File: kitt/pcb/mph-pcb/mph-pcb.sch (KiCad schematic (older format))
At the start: 99 parts, among them J1 Screw_Terminal_01x02, J2 Screw_Terminal_01x02, U1 TLC5940NT, U2 TLC5940NT, U3 TLC5940NT, U4 TLC5940NT, U5 TLC5940NT, U6 TLC5940NT, U7 TLC5940NT

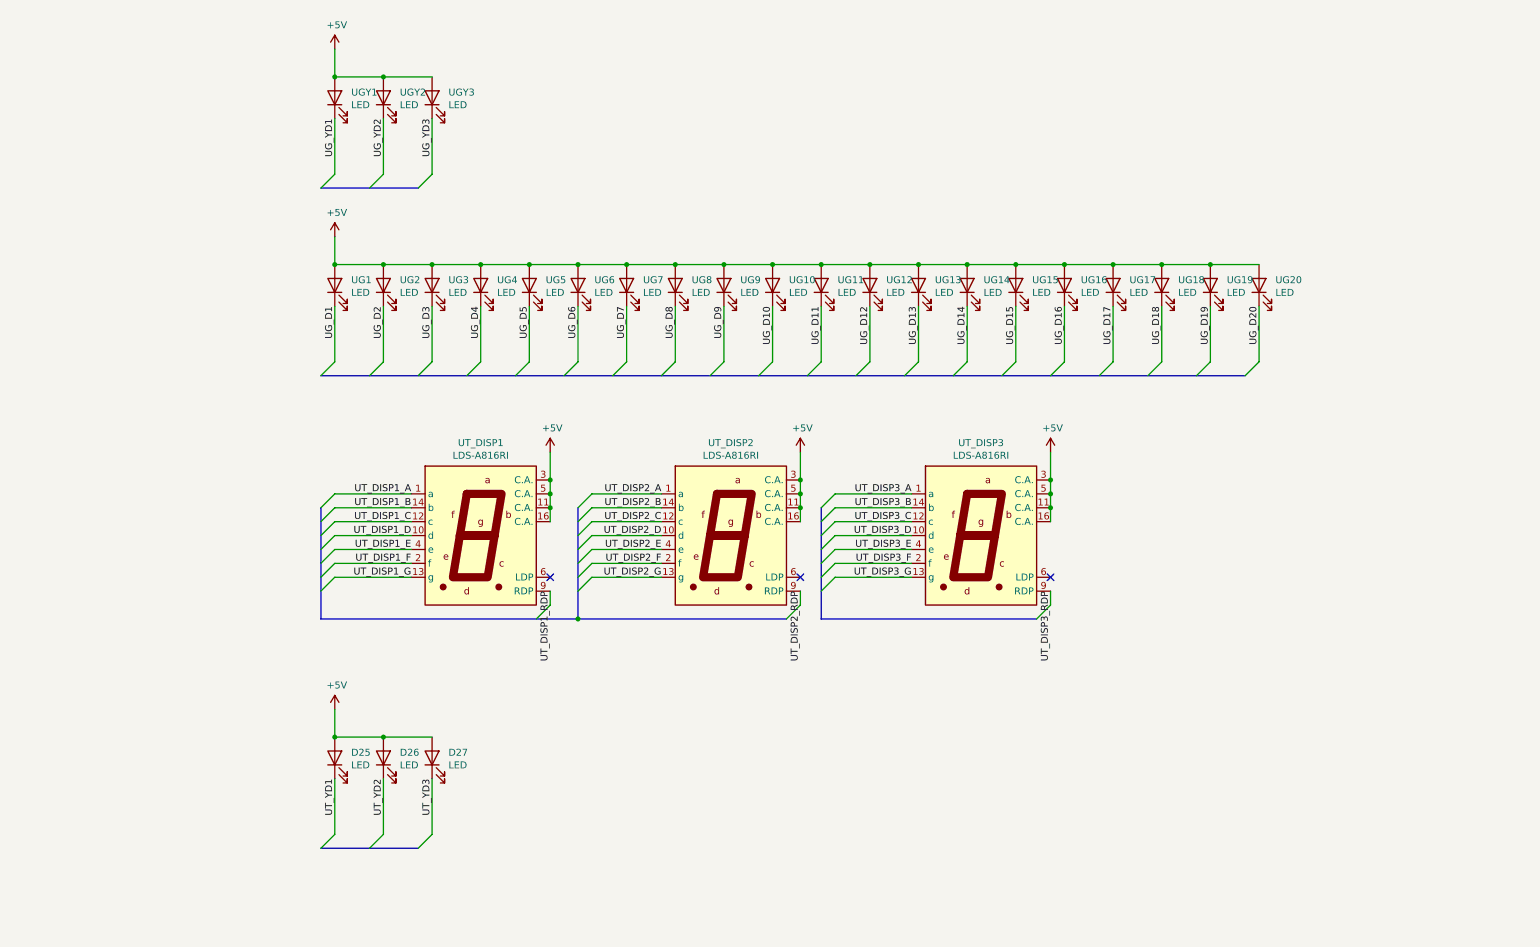
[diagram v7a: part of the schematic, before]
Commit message: added mph leds
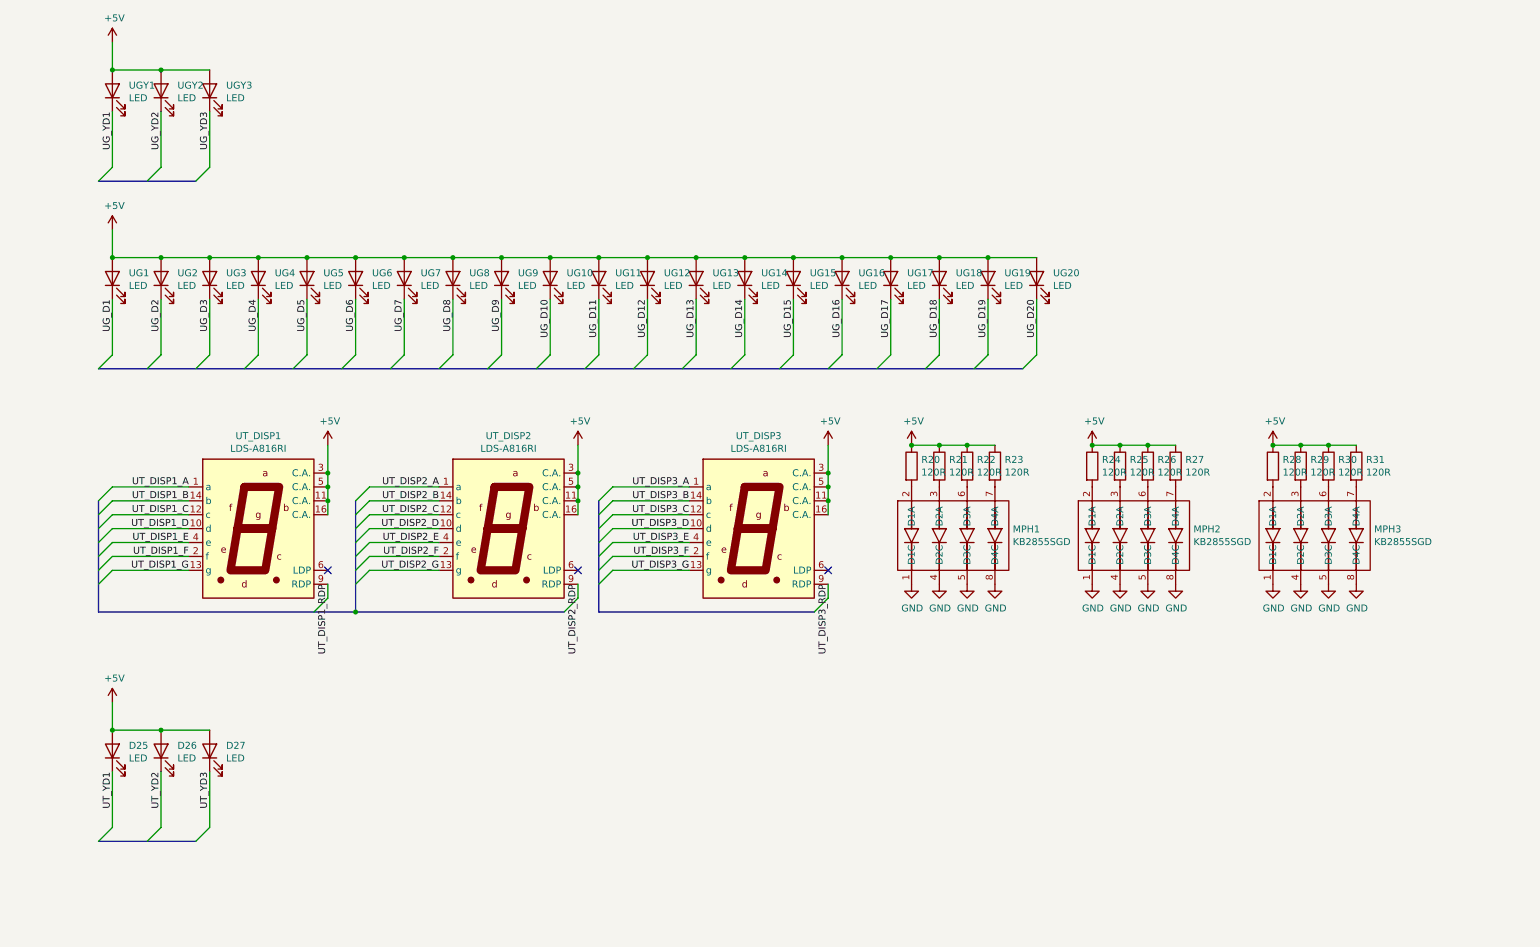
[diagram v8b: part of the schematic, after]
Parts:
- added MPH1, MPH2, MPH3: KB2855SGD, symbol KITT-Symbols:KB2855SGD
- added R20, R21, R22, R23, R24, R25, R26, R27, R28, R29, R30, R31: 120R, Resistor_THT:R_Axial_DIN0207_L6.3mm_D2.5mm_P10.16mm_Horizontal, symbol Device:R
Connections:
- net +5V: now also R20.1, R21.1, R22.1, R23.1, R24.1, R25.1, R26.1, R27.1, R28.1, R29.1, R30.1, R31.1
- net GND: now also MPH1.1 (D1C), MPH1.4 (D2C), MPH1.5 (D3C), MPH1.8 (D4C), MPH2.1 (D1C), MPH2.4 (D2C), MPH2.5 (D3C), MPH2.8 (D4C), MPH3.1 (D1C), MPH3.4 (D2C), MPH3.5 (D3C), MPH3.8 (D4C)
- new net: MPH1.2 (D1A), R20.2
- new net: MPH1.3 (D2A), R21.2
- new net: MPH1.6 (D3A), R22.2
- new net: MPH1.7 (D4A), R23.2
- new net: MPH2.2 (D1A), R24.2
- new net: MPH2.3 (D2A), R25.2
- new net: MPH2.6 (D3A), R26.2
- new net: MPH2.7 (D4A), R27.2
- new net: MPH3.2 (D1A), R28.2
- new net: MPH3.3 (D2A), R29.2
- new net: MPH3.6 (D3A), R30.2
- new net: MPH3.7 (D4A), R31.2
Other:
- moved on the sheet: D25, D26, D27, UG1, UG10, UG11, UG12, UG13, UG14, UG15, UG16, UG17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
